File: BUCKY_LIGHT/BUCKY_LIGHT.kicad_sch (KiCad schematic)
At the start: 98 parts, among them J1 LIGHT -> MAIN, Q1 Q_Photo_NPN, Q10 Q_Photo_NPN, Q11 Q_Photo_NPN, Q12 Q_Photo_NPN, Q13 Q_Photo_NPN, Q14 Q_Photo_NPN, Q15 Q_Photo_NPN, Q16 Q_Photo_NPN, Q17 Q_Photo_NPN, Q18 Q_Photo_NPN, Q19 Q_Photo_NPN, Q2 Q_Photo_NPN, Q20 Q_Photo_NPN, Q21 Q_Photo_NPN, Q22 Q_Photo_NPN, Q23 Q_Photo_NPN, Q24 Q_Photo_NPN, Q25 Q_Photo_NPN, Q26 Q_Photo_NPN, Q27 Q_Photo_NPN, Q28 Q_Photo_NPN, Q3 Q_Photo_NPN, Q4 Q_Photo_NPN, Q5 Q_Photo_NPN, Q6 Q_Photo_NPN, Q7 Q_Photo_NPN, Q8 Q_Photo_NPN, Q9 Q_Photo_NPN

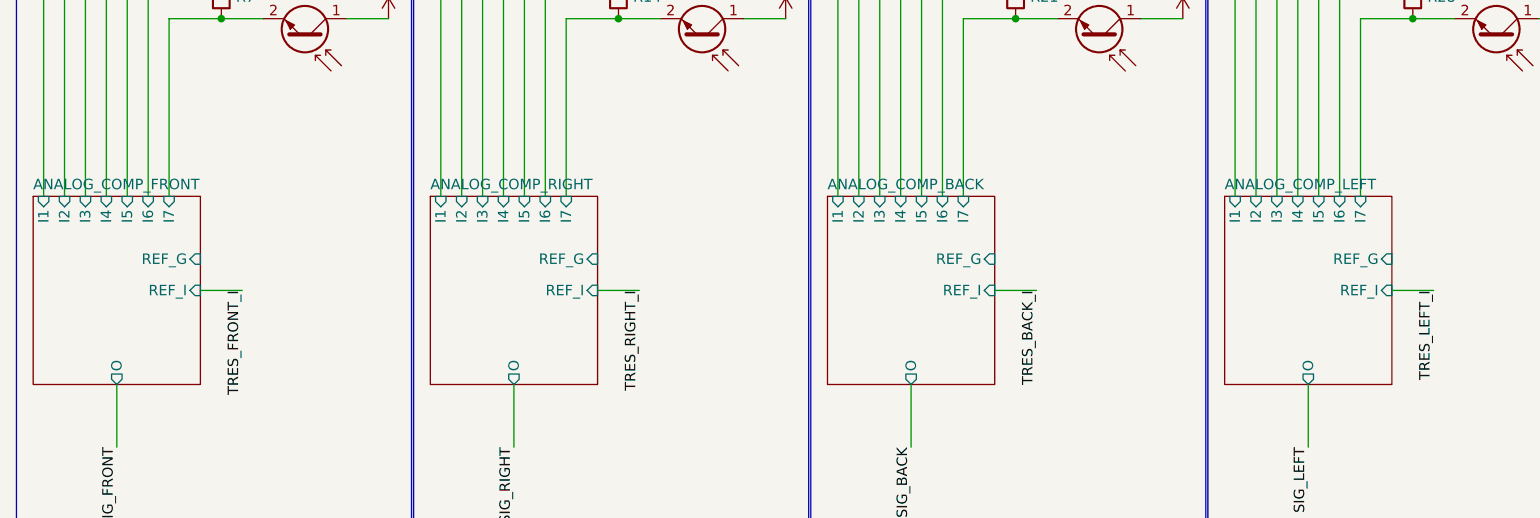
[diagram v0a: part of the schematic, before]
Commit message: chore: convert 2 layer DRIVE -> 4 layer
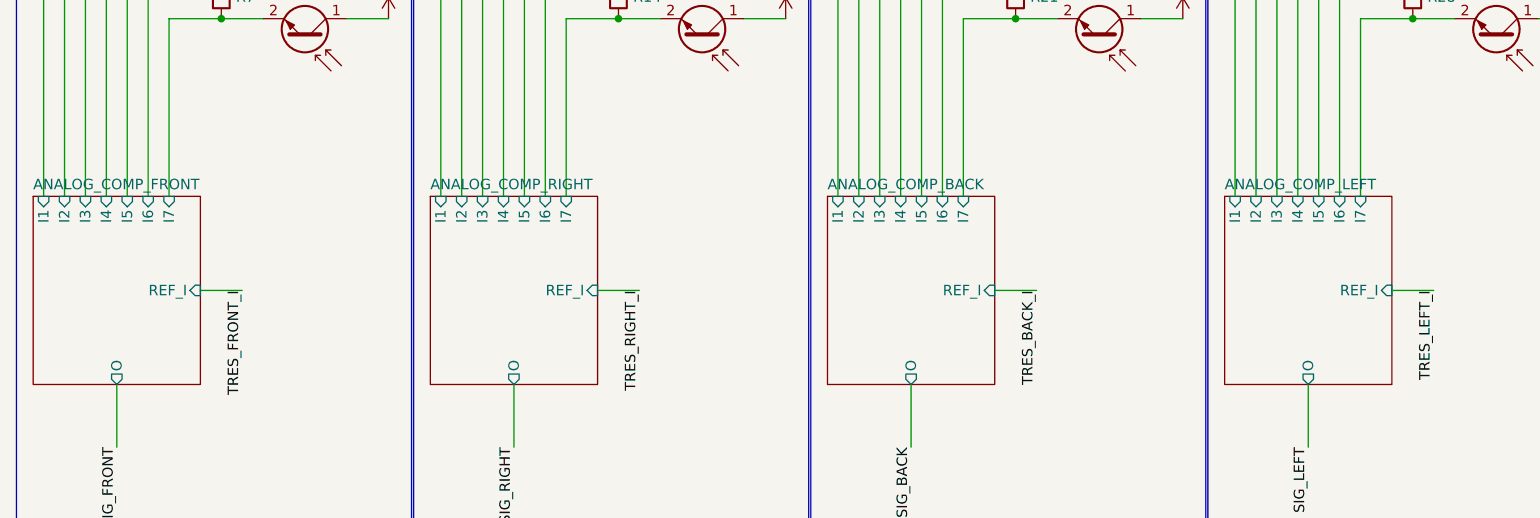
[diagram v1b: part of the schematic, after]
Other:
- sheet ANALOG_COMP_BACK ports: added none; removed REF_G
- sheet ANALOG_COMP_FRONT ports: added none; removed REF_G
- sheet ANALOG_COMP_LEFT ports: added none; removed REF_G
- sheet ANALOG_COMP_RIGHT ports: added none; removed REF_G
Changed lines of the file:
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@@
-			)
-		)
-		(pin "REF_G" input
-			(at 82.55 180.34 0)
-			(effects
-				(font
-					(size 1.27 1.27)
-				)
-				(justify right)
 			)
 		)
@@
 			)
 		)
-		(pin "REF_G" input
-			(at 179.07 180.34 0)
-			(effects
-				(font
-					(size 1.27 1.27)
-				)
-				(justify right)
-			)
-		)
 		(pin "O" output
 			(at 168.91 195.58 270)
@@
 			)
 		)
-		(pin "REF_G" input
-			(at 34.29 180.34 0)
-			(effects
-				(font
-					(size 1.27 1.27)
-				)
-				(justify right)
-			)
-		)
 		(pin "O" output
 			(at 24.13 195.58 270)
@@
 			(effects
 				(font
-					(size 1.27 1.27)
-				)
-				(justify right)
-			)
-		)
-		(pin "REF_G" input
-			(at 130.81 180.34 0)
-			(effects
-				(font

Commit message: chore: make all PCBs from 2 layers to 4 layers
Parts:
- R1, R10, R11, R12, R13, R14, R15, R16, R17, R18, R19, R2, R20, R21, R22, R23, R24, R25, R26, R27, R28, R29, R3, R30, R31, R32, R33, R35, R37, R39, R4, R5, R6, R7, R8, R9: footprint Resistor_SMD:R_0603_1608Metric -> Resistor_SMD:R_0805_2012Metric
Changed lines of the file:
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@@
 	(title_block
 		(title "BUCKY LIGHT")
-		(date "2024-05-09")
+		(date "2024-09-11")
 		(rev "V1")
 		(company "koen1711")
@@
 			)
 		)
-		(property "Footprint" "Resistor_SMD:R_0603_1608Metric"
+		(property "Footprint" "Resistor_SMD:R_0805_2012Metric"
 			(at 131.572 82.55 90)
 			(effects
@@
 			)
 		)
-		(property "Footprint" "Resistor_SMD:R_0603_1608Metric"
+		(property "Footprint" "Resistor_SMD:R_0805_2012Metric"
 			(at 131.572 107.95 90)
 			(effects
@@
 			)
 		)
-		(property "Footprint" "Resistor_SMD:R_0603_1608Metric"
+		(property "Footprint" "Resistor_SMD:R_0805_2012Metric"
 			(at 83.312 69.85 90)
 			(effects
@@
 			)
 		)
-		(property "Footprint" "Resistor_SMD:R_0603_1608Metric"
+		(property "Footprint" "Resistor_SMD:R_0805_2012Metric"
 			(at 131.572 95.25 90)
 			(effects
@@
 			)
 		)
-		(property "Footprint" "Resistor_SMD:R_0603_1608Metric"
+		(property "Footprint" "Resistor_SMD:R_0805_2012Metric"
 			(at 173.99 39.878 90)
 			(effects
@@
 			)
 		)
-		(property "Footprint" "Resistor_SMD:R_0603_1608Metric"
+		(property "Footprint" "Resistor_SMD:R_0805_2012Metric"
 			(at 131.572 147.32 90)
 			(effects
@@
 			)
 		)
-		(property "Footprint" "Resistor_SMD:R_0603_1608Metric"
+		(property "Footprint" "Resistor_SMD:R_0805_2012Metric"
 			(at 35.052 120.65 90)
 			(effects
@@
 			)
 		)
-		(property "Footprint" "Resistor_SMD:R_0603_1608Metric"
+		(property "Footprint" "Resistor_SMD:R_0805_2012Metric"
 			(at 179.832 107.95 90)
 			(effects
@@
 			)
 		)
-		(property "Footprint" "Resistor_SMD:R_0603_1608Metric"
+		(property "Footprint" "Resistor_SMD:R_0805_2012Metric"
 			(at 131.572 133.35 90)
 			(effects
@@
 			)
 		)
-		(property "Footprint" "Resistor_SMD:R_0603_1608Metric"
+		(property "Footprint" "Resistor_SMD:R_0805_2012Metric"
 			(at 131.572 120.65 90)
 			(effects
@@
 			)
 		)
-		(property "Footprint" "Resistor_SMD:R_0603_1608Metric"
+		(property "Footprint" "Resistor_SMD:R_0805_2012Metric"
 			(at 73.66 39.878 90)
 			(effects
@@
 			)
 		)
-		(property "Footprint" "Resistor_SMD:R_0603_1608Metric"
+		(property "Footprint" "Resistor_SMD:R_0805_2012Metric"
 			(at 179.832 147.32 90)
 			(effects
@@
 			)
 		)
-		(property "Footprint" "Resistor_SMD:R_0603_1608Metric"
+		(property "Footprint" "Resistor_SMD:R_0805_2012Metric"
 			(at 83.312 133.35 90)
 			(effects
@@
 			)
 		)
-		(property "Footprint" "Resistor_SMD:R_0603_1608Metric"
+		(property "Footprint" "Resistor_SMD:R_0805_2012Metric"
 			(at 35.052 107.95 90)
 			(effects
@@
 			)
 		)
-		(property "Footprint" "Resistor_SMD:R_0603_1608Metric"
+		(property "Footprint" "Resistor_SMD:R_0805_2012Metric"
 			(at 83.312 120.65 90)
 			(effects
@@
 			)
 		)
-		(property "Footprint" "Resistor_SMD:R_0603_1608Metric"
+		(property "Footprint" "Resistor_SMD:R_0805_2012Metric"
 			(at 179.832 69.85 90)
 			(effects
@@
 			)
 		)
-		(property "Footprint" "Resistor_SMD:R_0603_1608Metric"
+		(property "Footprint" "Resistor_SMD:R_0805_2012Metric"
 			(at 123.19 39.878 90)
 			(effects
@@
 			)
 		)
-		(property "Footprint" "Resistor_SMD:R_0603_1608Metric"
+		(property "Footprint" "Resistor_SMD:R_0805_2012Metric"
 			(at 222.25 44.958 90)
 			(effects
@@
 			)
 		)
-		(property "Footprint" "Resistor_SMD:R_0603_1608Metric"
+		(property "Footprint" "Resistor_SMD:R_0805_2012Metric"
 			(at 83.312 95.25 90)
 			(effects
@@
 			)
 		)
-		(property "Footprint" "Resistor_SMD:R_0603_1608Metric"
+		(property "Footprint" "Resistor_SMD:R_0805_2012Metric"
 			(at 35.052 133.35 90)
 			(effects
@@
 			)
 		)
-		(property "Footprint" "Resistor_SMD:R_0603_1608Metric"
+		(property "Footprint" "Resistor_SMD:R_0805_2012Metric"
 			(at 179.832 82.55 90)
 			(effects
@@
 			)
 		)
-		(property "Footprint" "Resistor_SMD:R_0603_1608Metric"
+		(property "Footprint" "Resistor_SMD:R_0805_2012Metric"
 			(at 179.832 133.35 90)
 			(effects
@@
 			)
 		)
-		(property "Footprint" "Resistor_SMD:R_0603_1608Metric"
+		(property "Footprint" "Resistor_SMD:R_0805_2012Metric"
 			(at 179.832 95.25 90)
 			(effects
@@
 			)
 		)
-		(property "Footprint" "Resistor_SMD:R_0603_1608Metric"
+		(property "Footprint" "Resistor_SMD:R_0805_2012Metric"
 			(at 222.25 19.558 90)
 			(effects
@@
 			)
 		)
-		(property "Footprint" "Resistor_SMD:R_0603_1608Metric"
+		(property "Footprint" "Resistor_SMD:R_0805_2012Metric"
 			(at 83.312 147.32 90)
 			(effects
@@
 			)
 		)
-		(property "Footprint" "Resistor_SMD:R_0603_1608Metric"
+		(property "Footprint" "Resistor_SMD:R_0805_2012Metric"
 			(at 35.052 95.25 90)
 			(effects
@@
 			)
 		)
-		(property "Footprint" "Resistor_SMD:R_0603_1608Metric"
+		(property "Footprint" "Resistor_SMD:R_0805_2012Metric"
 			(at 222.25 32.258 90)
 			(effects
@@
 			)
 		)
-		(property "Footprint" "Resistor_SMD:R_0603_1608Metric"
+		(property "Footprint" "Resistor_SMD:R_0805_2012Metric"
 			(at 83.312 107.95 90)
 			(effects
@@
 			)
 		)
-		(property "Footprint" "Resistor_SMD:R_0603_1608Metric"
+		(property "Footprint" "Resistor_SMD:R_0805_2012Metric"
 			(at 35.052 69.85 90)
 			(effects
@@
 			)
 		)
-		(property "Footprint" "Resistor_SMD:R_0603_1608Metric"
+		(property "Footprint" "Resistor_SMD:R_0805_2012Metric"
 			(at 24.13 39.878 90)
 			(effects
@@
 			)
 		)
-		(property "Footprint" "Resistor_SMD:R_0603_1608Metric"
+		(property "Footprint" "Resistor_SMD:R_0805_2012Metric"
 			(at 131.572 69.85 90)
 			(effects
@@
 			)
 		)
-		(property "Footprint" "Resistor_SMD:R_0603_1608Metric"
+		(property "Footprint" "Resistor_SMD:R_0805_2012Metric"
 			(at 35.052 147.32 90)
 			(effects
@@
 			)
 		)
-		(property "Footprint" "Resistor_SMD:R_0603_1608Metric"
+		(property "Footprint" "Resistor_SMD:R_0805_2012Metric"
 			(at 35.052 82.55 90)
 			(effects
@@
 			)
 		)
-		(property "Footprint" "Resistor_SMD:R_0603_1608Metric"
+		(property "Footprint" "Resistor_SMD:R_0805_2012Metric"
 			(at 222.25 57.658 90)
 			(effects
@@
 			)
 		)
-		(property "Footprint" "Resistor_SMD:R_0603_1608Metric"
+		(property "Footprint" "Resistor_SMD:R_0805_2012Metric"
 			(at 83.312 82.55 90)
 			(effects
@@
 			)
 		)
-		(property "Footprint" "Resistor_SMD:R_0603_1608Metric"
+		(property "Footprint" "Resistor_SMD:R_0805_2012Metric"
 			(at 179.832 120.65 90)
 			(effects

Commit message: fix: BUCKY_MAIN v2?
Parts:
- added R34, R36, R38, R40, R41, R42, R43, R44, R45, R46, R47, R48, R49, R50, R51, R52, R53, R54, R55, R56: 10k, Resistor_SMD:R_0805_2012Metric, symbol Device:R
- added R57, R58, R59, R60: 20k, Resistor_SMD:R_0805_2012Metric, symbol Device:R
- R33, R35, R37, R39: value 20k -> 10k
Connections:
- net +5V: now also R34.1, R36.1, R38.1, R40.1, R41.1, R42.1, R43.1, R44.1, R45.1, R46.1, R47.1, R48.1, R49.1, R50.1, R51.1, R52.1, R53.1, R54.1, R55.1, R56.1, R57.1, R58.1, R59.1, R60.1
- net TRES_BACK_I: now also R58.2; no longer R35.2
- net TRES_FRONT_I: now also R57.2; no longer R33.2
- net TRES_LEFT_I: now also R59.2; no longer R37.2
- net TRES_RIGHT_I: now also R60.2; no longer R39.2
- new net: L18.2 (A), R46.2
- new net: L21.2 (A), R49.2
- new net: L12.2 (A), R40.2
- new net: L23.2 (A), R51.2
- new net: L24.2 (A), R52.2
- new net: L2.2 (A), R30.2
- new net: L15.2 (A), R43.2
- new net: L13.2 (A), R41.2
- new net: L6.2 (A), R34.2
- new net: L28.2 (A), R56.2
- new net: L27.2 (A), R55.2
- new net: L20.2 (A), R48.2
- new net: L22.2 (A), R50.2
- new net: L8.2 (A), R36.2
- new net: L26.2 (A), R54.2
- new net: L10.2 (A), R38.2
- new net: L16.2 (A), R44.2
- new net: L3.2 (A), R31.2
- new net: L9.2 (A), R37.2
- new net: L14.2 (A), R42.2
- new net: L1.2 (A), R29.2
- new net: L11.2 (A), R39.2
- new net: L7.2 (A), R35.2
- new net: L19.2 (A), R47.2
- new net: L17.2 (A), R45.2
- new net: L4.2 (A), R32.2
- new net: L5.2 (A), R33.2
- new net: L25.2 (A), R53.2
